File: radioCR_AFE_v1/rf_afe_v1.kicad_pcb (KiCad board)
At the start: 2 copper layers, 122.5 x 36.9 mm, 39 parts, among them J1 Conn_Coaxial, J2 Conn_Coaxial, U1 PHA-13LN, U3 PHA-13LN

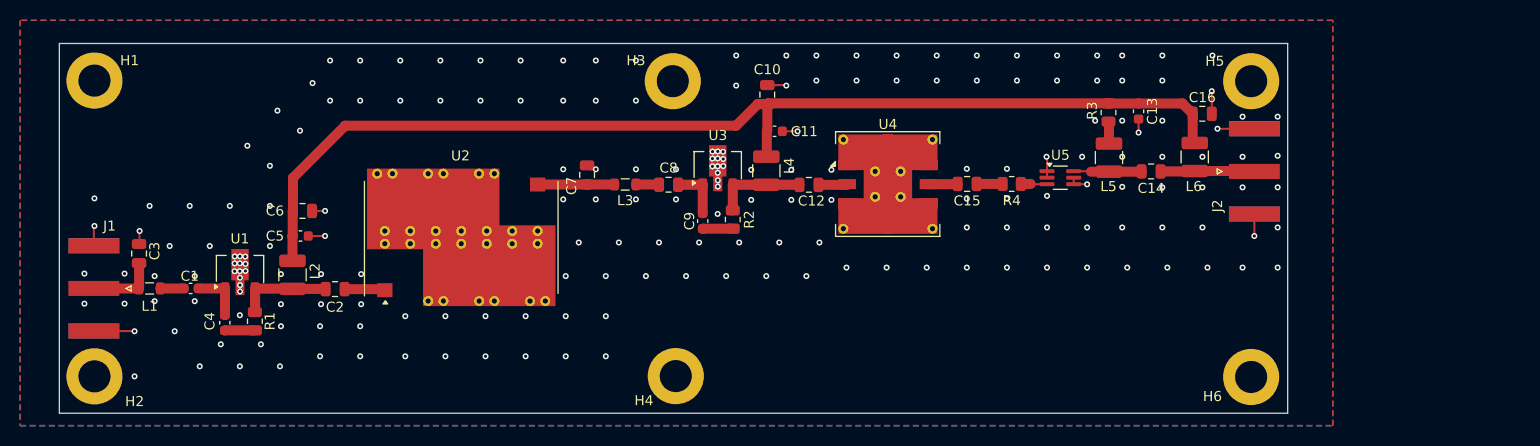
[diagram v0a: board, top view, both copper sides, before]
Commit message: attenuator added to schematic and PCB
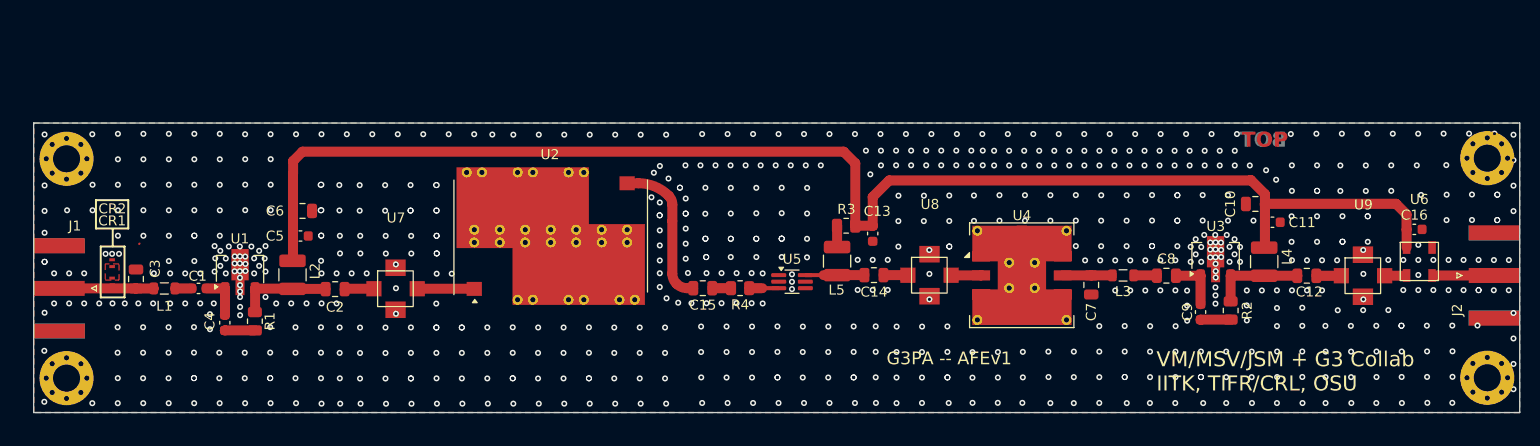
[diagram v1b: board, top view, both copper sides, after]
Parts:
- removed H3, H4: MountingHole_Pad, MountingHole:MountingHole_3.2mm_M3_DIN965_Pad
- removed L6: L_Small, Inductor_SMD:L_1210_3225Metric
- added CR1: SP3031-01ETG, SP3021:SOD882_LTF, F.Cu at (94.8, 99.0)
- added CR2: SP3031-01ETG, SP3021:SOD882_LTF, F.Cu at (94.8, 97.2)
- added U6: TCBT-6G+, minickts_kicad:GU1604, F.Cu at (225.1, 97.0)
- added U7: PAT-3, minickts_kicad:PAT-3+, F.Cu at (123.0, 99.8)
- added U8: PAT-3, minickts_kicad:PAT-3+, F.Cu at (176.3, 98.4)
- added U9: PAT-3, minickts_kicad:PAT-3+, F.Cu at (219.5, 98.5)
- C1, C12, C2: value C_Small -> 2.2 uF
- C10, C6: value C_Small -> 10 uF
- C11, C5: value C_Small -> 1 nF
- C13, C4, C9: value C_Small -> 0.1 uF
- C14, C15: value C_Small -> 2.4 nF
- C16: value C_Small -> 0.01 uF; footprint Capacitor_SMD:C_0805_2012Metric -> Capacitor_SMD:C_0603_1608Metric
- C3, C7: value C_Small -> 1.5 pF
- C8: value C_Small -> 2.2u F
- H1, H2, H5, H6: footprint MountingHole:MountingHole_3.2mm_M3_DIN965_Pad -> MountingHole:MountingHole_2.7mm_M2.5_Pad_Via
- L1, L3: value L_Small -> 6.2 nH
- L2, L4, L5: value L_Small -> 15 uH
- R1, R2: value R_Small -> 1.5k
- R3: value R_Small -> 36.5
- R4: value R_Small -> 10
- U2: value ~ -> BSF108+
- U4: value ~ -> RBP188
- U5: value ~ -> PSA8A+
- moved C7 51.5 mm to (192.4, 99.4), turned to 90 degrees
- moved C12 50.5 mm to (213.9, 98.5)
- moved C8 50.5 mm to (199.9, 98.5)
- moved C9 50.5 mm to (203.3, 102.1)
- moved L3 50.5 mm to (195.6, 98.4)
- moved L4 50.5 mm to (209.7, 97.1)
- moved R2 50.5 mm to (206.3, 101.9)
- moved U3 50.5 mm to (204.8, 96.5)
- moved C11 50.5 mm to (210.5, 93.1)
- moved C10 49.9 mm to (208.8, 91.3), turned to 180 degrees
- moved C14 29.5 mm to (170.7, 98.4)
- moved C13 29.2 mm to (170.6, 94.3)
- moved R4 29.0 mm to (157.4, 99.7)
- moved L5 29.0 mm to (167.1, 97.0)
- moved U5 28.7 mm to (162.6, 99.1)
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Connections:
- C12 pad 2: Net-(U4-RF_IN) -> Net-(U9-INP)
- C14 pad 1: Net-(J2-In) -> Net-(U8-INP)
- C15 pad 2: Net-(U4-RF_OUT) -> Net-(U2-RFOUT)
- C16 pad 1: GND -> +5V
- C16 pad 2: +5V -> GND
- C2 pad 2: Net-(U2-RFIN) -> Net-(U7-INP)
- C7 pad 2: Net-(U2-RFOUT) -> Net-(U4-RF_OUT)
- L3 pad 1: Net-(U2-RFOUT) -> Net-(U4-RF_OUT)
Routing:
- net +5V: track 109.9 -> 141.6 mm
- net GND: track 28.5 -> 0.07 mm, vias 201 -> 723
- net Net-(U2-RFOUT): track 7.68 -> 15.2 mm
- net Net-(J2-In): track 9.32 -> 5.41 mm
- net Net-(U7-INP): track 0.00 -> 2.94 mm
- net Net-(U9-INP): track 0.00 -> 2.49 mm
- net Net-(U8-INP): track 0.00 -> 2.43 mm
- net Net-(J1-In): track 7.03 -> 9.44 mm
- net Net-(U4-RF_OUT): track 2.89 -> 4.89 mm
- net Net-(U6-RF): track 0.00 -> 1.83 mm
- net Net-(U2-RFIN): track 4.05 -> 5.70 mm
- net Net-(U5-RF-OUT/Vdd): track 6.80 -> 5.89 mm
- net Net-(C1-Pad2): track 5.30 -> 4.51 mm
- net Net-(C15-Pad1): track 2.59 -> 1.86 mm
- net Net-(C1-Pad1): track 2.35 -> 1.67 mm
- added copper zone on F.Cu, net GND
- added copper zone on F.Cu, net Net-(CR1-Pad2)
- removed copper zone on F.Cu, net (none)
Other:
- board size 122.5 x 36.9 mm -> 148.2 x 28.9 mm
- board text added: "BOT"
- board text added: "G3PA -- AFEv1"
- board text added: "TOP"
- board text added: "VM/MSV/JSM + G3 Collab IITK, TIFR/CRL, OSU"
